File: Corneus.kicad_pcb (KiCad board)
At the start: 2 copper layers, 262 x 112 mm, 155 parts, among them J1 USB_B_Micro, Q1 Q_NPN_BCE, SW1 SW_Push, U1 ATmega32U4-AU, U2 PRTR5V0U2X, Y1 16MHz

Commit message: rerouted columns
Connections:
- U1 pad 25: Net-(U1-Pad25) -> COL4
- U1 pad 26: Net-(U1-Pad26) -> COL5
- U1 pad 27: Net-(U1-Pad27) -> COL3
- U1 pad 28: Net-(U1-Pad28) -> COL2
- U1 pad 29: Net-(U1-Pad29) -> COL1
- U1 pad 30: Net-(U1-Pad30) -> COL0
- U1 pad 36: Net-(U1-Pad36) -> COL11
- U1 pad 37: Net-(U1-Pad37) -> COL10
- U1 pad 38: Net-(U1-Pad38) -> COL9
- U1 pad 39: Net-(U1-Pad39) -> COL6
- U1 pad 40: Net-(U1-Pad40) -> COL7
- U1 pad 41: Net-(U1-Pad41) -> COL8
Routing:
- net COL0: track 40.8 -> 202.6 mm, vias 0 -> 1
- net COL11: track 40.8 -> 193.8 mm, vias 0 -> 5
- net COL1: track 40.8 -> 185.9 mm, vias 0 -> 1
- net COL2: track 40.8 -> 178.1 mm, vias 0 -> 3
- net COL10: track 40.8 -> 173.1 mm, vias 0 -> 5
- net COL9: track 40.8 -> 164.8 mm, vias 0 -> 5
- net COL3: track 69.8 -> 166.1 mm, vias 0 -> 1
- net COL8: track 69.8 -> 117.8 mm, vias 0 -> 3
- net COL4: track 67.0 -> 112.7 mm, vias 0 -> 1
- net COL7: track 70.0 -> 96.4 mm, vias 0 -> 3
- net COL5: track 71.8 -> 93.9 mm, vias 0 -> 1
- net COL6: track 77.0 -> 89.3 mm, vias 0 -> 1
- net VCC: track 9.51 -> 13.1 mm
- net LEDGND: track 955.0 -> 952.9 mm, vias 8 -> 10

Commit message: add ground fills, adjust some traces to improve clearance
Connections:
- U1 pad 31: Net-(U1-Pad31) -> LEDPWM
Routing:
- net LEDPWM: track 0.00 -> 82.8 mm, vias 0 -> 2
- net GND: track 1.59 -> 43.1 mm, vias 0 -> 22
- net +5V: track 1153.6 -> 1194.7 mm, vias 36 -> 37
- net LEDGND: track 952.9 -> 956.1 mm
- net ROW3: track 189.8 -> 192.8 mm
- added copper zone on B.Cu, net GND
- added copper zone on F.Cu, net GND
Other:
- rule via_min_size: 0.6 -> 0.2

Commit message: added tooling holes
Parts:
- added REF**: JLCPCB_tooling_hole, Choco617_parts:JLCPCB_tooling_hole, F.Cu at (276.4, 52.5)
- added REF**: JLCPCB_tooling_hole, Choco617_parts:JLCPCB_tooling_hole, F.Cu at (168.9, 159.5)
- added REF**: JLCPCB_tooling_hole, Choco617_parts:JLCPCB_tooling_hole, F.Cu at (128.0, 159.5)
- added e: JLCPCB_tooling_hole, Choco617_parts:JLCPCB_tooling_hole, F.Cu at (20.4, 52.5)

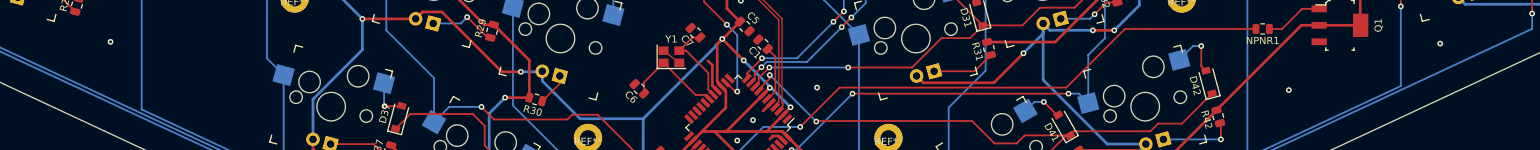
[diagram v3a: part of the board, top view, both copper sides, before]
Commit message: added name/rev/repo details on silkscreen layer
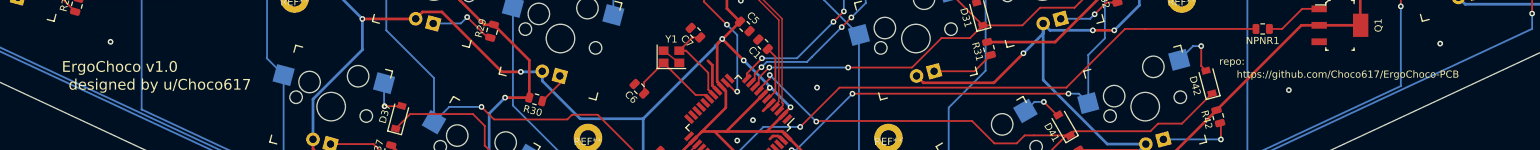
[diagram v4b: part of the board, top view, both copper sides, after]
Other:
- board text added: "ErgoChoco v1.0"
- board text added: "designed by u/Choco617"
- board text added: "https://github.com/Choco617/ErgoChoco-PCB"
- board text added: "repo:"
